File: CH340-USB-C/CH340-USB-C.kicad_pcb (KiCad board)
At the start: 2 copper layers, 37.2 x 19.5 mm, 25 parts, among them J1 USB_C_Receptacle_USB2.0, J2 Conn_01x05_Female, SW1 SW_Push_SPDT, U1 XC6206PxxxMR, U2 CH340N

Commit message: fix 電路板零件屬性及用料
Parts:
- U1: value XC6206PxxxMR -> XC6206P332MR
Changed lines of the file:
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@@
     (property "Sheetfile" "CH340-USB-C.kicad_sch")
     (property "Sheetname" "")
-    (attr exclude_from_pos_files)
+    (property "exclude_from_bom" "")
+    (attr exclude_from_pos_files exclude_from_bom)
     (fp_text reference "TP2" (at 0 -1.998) (layer "F.SilkS") hide
       (effects (font (size 1 1) (thickness 0.15)))
@@
     (property "Sheetfile" "CH340-USB-C.kicad_sch")
     (property "Sheetname" "")
-    (attr exclude_from_pos_files)
+    (property "exclude_from_bom" "")
+    (attr exclude_from_pos_files exclude_from_bom)
     (fp_text reference "TP6" (at 0 -1.998) (layer "F.SilkS") hide
       (effects (font (size 1 1) (thickness 0.15)))
@@
     (fp_line (start 1 -0.625) (end 1 0.625) (layer "F.Fab") (width 0.1))
     (fp_line (start -1 -0.625) (end 1 -0.625) (layer "F.Fab") (width 0.1))
-    (pad "1" smd roundrect (at -0.9125 0) (size 1.025 1.4) (layers "F.Cu" "F.Paste" "F.Mask") (roundrect_rratio 0.243902)
+    (pad "1" smd roundrect (at -0.9125 0) (size 1.025 1.4) (layers "F.Cu" "F.Paste" "F.Mask") (roundrect_rratio 0.243902439)
       (net 10 "Net-(D3-Pad2)") (pintype "passive"))
-    (pad "2" smd roundrect (at 0.9125 0) (size 1.025 1.4) (layers "F.Cu" "F.Paste" "F.Mask") (roundrect_rratio 0.243902)
+    (pad "2" smd roundrect (at 0.9125 0) (size 1.025 1.4) (layers "F.Cu" "F.Paste" "F.Mask") (roundrect_rratio 0.243902439)
       (net 4 "VCC") (pintype "passive"))
     (model "${KICAD6_3DMODEL_DIR}/Resistor_SMD.3dshapes/R_0805_2012Metric.wrl"
@@
     (fp_line (start 1 -0.625) (end 1 0.625) (layer "F.Fab") (width 0.1))
     (fp_line (start -1 0.625) (end -1 -0.625) (layer "F.Fab") (width 0.1))
-    (pad "1" smd roundrect (at -0.9125 0 180) (size 1.025 1.4) (layers "F.Cu" "F.Paste" "F.Mask") (roundrect_rratio 0.243902)
+    (pad "1" smd roundrect (at -0.9125 0 180) (size 1.025 1.4) (layers "F.Cu" "F.Paste" "F.Mask") (roundrect_rratio 0.243902439)
       (net 2 "GND") (pintype "passive"))
-    (pad "2" smd roundrect (at 0.9125 0 180) (size 1.025 1.4) (layers "F.Cu" "F.Paste" "F.Mask") (roundrect_rratio 0.243902)
+    (pad "2" smd roundrect (at 0.9125 0 180) (size 1.025 1.4) (layers "F.Cu" "F.Paste" "F.Mask") (roundrect_rratio 0.243902439)
       (net 16 "/CC2") (pintype "passive"))
     (model "${KICAD6_3DMODEL_DIR}/Resistor_SMD.3dshapes/R_0805_2012Metric.wrl"
@@
     (property "Sheetfile" "CH340-USB-C.kicad_sch")
     (property "Sheetname" "")
-    (attr exclude_from_pos_files)
+    (property "exclude_from_bom" "")
+    (attr exclude_from_pos_files exclude_from_bom)
     (fp_text reference "TP5" (at 0 -1.998) (layer "F.SilkS") hide
       (effects (font (size 1 1) (thickness 0.15)))
@@
     (fp_line (start -1 -0.625) (end 1 -0.625) (layer "F.Fab") (width 0.1))
     (fp_line (start 1 -0.625) (end 1 0.625) (layer "F.Fab") (width 0.1))
-    (pad "1" smd roundrect (at -0.9125 0 180) (size 1.025 1.4) (layers "F.Cu" "F.Paste" "F.Mask") (roundrect_rratio 0.243902)
+    (pad "1" smd roundrect (at -0.9125 0 180) (size 1.025 1.4) (layers "F.Cu" "F.Paste" "F.Mask") (roundrect_rratio 0.243902439)
       (net 2 "GND") (pintype "passive"))
-    (pad "2" smd roundrect (at 0.9125 0 180) (size 1.025 1.4) (layers "F.Cu" "F.Paste" "F.Mask") (roundrect_rratio 0.243902)
+    (pad "2" smd roundrect (at 0.9125 0 180) (size 1.025 1.4) (layers "F.Cu" "F.Paste" "F.Mask") (roundrect_rratio 0.243902439)
       (net 12 "/CC1") (pintype "passive"))
     (model "${KICAD6_3DMODEL_DIR}/Resistor_SMD.3dshapes/R_0805_2012Metric.wrl"
@@
     (descr "SOT, 3 Pin (https://www.jedec.org/system/files/docs/to-236h.pdf variant AB), generated with kicad-footprint-generator ipc_gullwing_generator.py")
     (tags "SOT TO_SOT_SMD")
-    (property "LCSC" "C161345")
+    (property "LCSC" "C5446")
     (property "Sheetfile" "CH340-USB-C.kicad_sch")
     (property "Sheetname" "")
@@
       (effects (font (size 1 1) (thickness 0.15)))
     )
-    (fp_text value "XC6206PxxxMR" (at -4.8225 -0.623332 180) (layer "F.Fab")
+    (fp_text value "XC6206P332MR" (at -4.8225 -0.623332 180) (layer "F.Fab")
       (effects (font (size 1 1) (thickness 0.15)))
     )
@@
     (property "Sheetfile" "CH340-USB-C.kicad_sch")
     (property "Sheetname" "")
-    (attr exclude_from_pos_files)
+    (property "exclude_from_bom" "")
+    (attr exclude_from_pos_files exclude_from_bom)
     (fp_text reference "TP1" (at 0 -1.998) (layer "F.SilkS") hide
       (effects (font (size 1 1) (thickness 0.15)))
@@
     (fp_line (start 1 0.625) (end -1 0.625) (layer "F.Fab") (width 0.1))
     (fp_line (start -1 0.625) (end -1 -0.625) (layer "F.Fab") (width 0.1))
-    (pad "1" smd roundrect (at -0.9125 0) (size 1.025 1.4) (layers "F.Cu" "F.Paste" "F.Mask") (roundrect_rratio 0.243902)
+    (pad "1" smd roundrect (at -0.9125 0) (size 1.025 1.4) (layers "F.Cu" "F.Paste" "F.Mask") (roundrect_rratio 0.243902439)
       (net 6 "Net-(D1-Pad2)") (pintype "passive"))
-    (pad "2" smd roundrect (at 0.9125 0) (size 1.025 1.4) (layers "F.Cu" "F.Paste" "F.Mask") (roundrect_rratio 0.243902)
+    (pad "2" smd roundrect (at 0.9125 0) (size 1.025 1.4) (layers "F.Cu" "F.Paste" "F.Mask") (roundrect_rratio 0.243902439)
       (net 4 "VCC") (pintype "passive"))
     (model "${KICAD6_3DMODEL_DIR}/Resistor_SMD.3dshapes/R_0805_2012Metric.wrl"
@@
     (property "Sheetfile" "CH340-USB-C.kicad_sch")
     (property "Sheetname" "")
-    (attr exclude_from_pos_files)
+    (property "exclude_from_bom" "")
+    (attr exclude_from_pos_files exclude_from_bom)
     (fp_text reference "TP4" (at 0 -1.998) (layer "F.SilkS") hide
       (effects (font (size 1 1) (thickness 0.15)))
@@
     (property "Sheetfile" "CH340-USB-C.kicad_sch")
     (property "Sheetname" "")
-    (attr exclude_from_pos_files)
+    (property "exclude_from_bom" "")
+    (attr exclude_from_pos_files exclude_from_bom)
     (fp_text reference "TP3" (at 0 -1.998) (layer "F.SilkS") hide
       (effects (font (size 1 1) (thickness 0.15)))
@@
     (fp_line (start -1 0.625) (end -1 -0.625) (layer "F.Fab") (width 0.1))
     (fp_line (start 1 0.625) (end -1 0.625) (layer "F.Fab") (width 0.1))
-    (pad "1" smd roundrect (at -0.9125 0) (size 1.025 1.4) (layers "F.Cu" "F.Paste" "F.Mask") (roundrect_rratio 0.243902)
+    (pad "1" smd roundrect (at -0.9125 0) (size 1.025 1.4) (layers "F.Cu" "F.Paste" "F.Mask") (roundrect_rratio 0.243902439)
       (net 8 "Net-(D2-Pad2)") (pintype "passive"))
-    (pad "2" smd roundrect (at 0.9125 0) (size 1.025 1.4) (layers "F.Cu" "F.Paste" "F.Mask") (roundrect_rratio 0.243902)
+    (pad "2" smd roundrect (at 0.9125 0) (size 1.025 1.4) (layers "F.Cu" "F.Paste" "F.Mask") (roundrect_rratio 0.243902439)
       (net 4 "VCC") (pintype "passive"))
     (model "${KICAD6_3DMODEL_DIR}/Resistor_SMD.3dshapes/R_0805_2012Metric.wrl"
@@
     (descr "KiCad Logo")
     (tags "Logo KiCad")
-    (attr exclude_from_pos_files exclude_from_bom)
+    (attr board_only exclude_from_pos_files exclude_from_bom)
     (fp_text reference "REF**" (at 0 5.08) (layer "B.SilkS") hide
       (effects (font (size 1 1) (thickness 0.15)) (justify mirror))
@@
     (property "Sheetfile" "CH340-USB-C.kicad_sch")
     (property "Sheetname" "")
-    (attr smd)
+    (property "exclude_from_bom" "")
+    (attr smd exclude_from_pos_files exclude_from_bom)
     (fp_text reference "J2" (at -11.384 -12.34 unlocked) (layer "B.SilkS")
       (effects (font (size 1 1) (thickness 0.15)) (justify mirror))

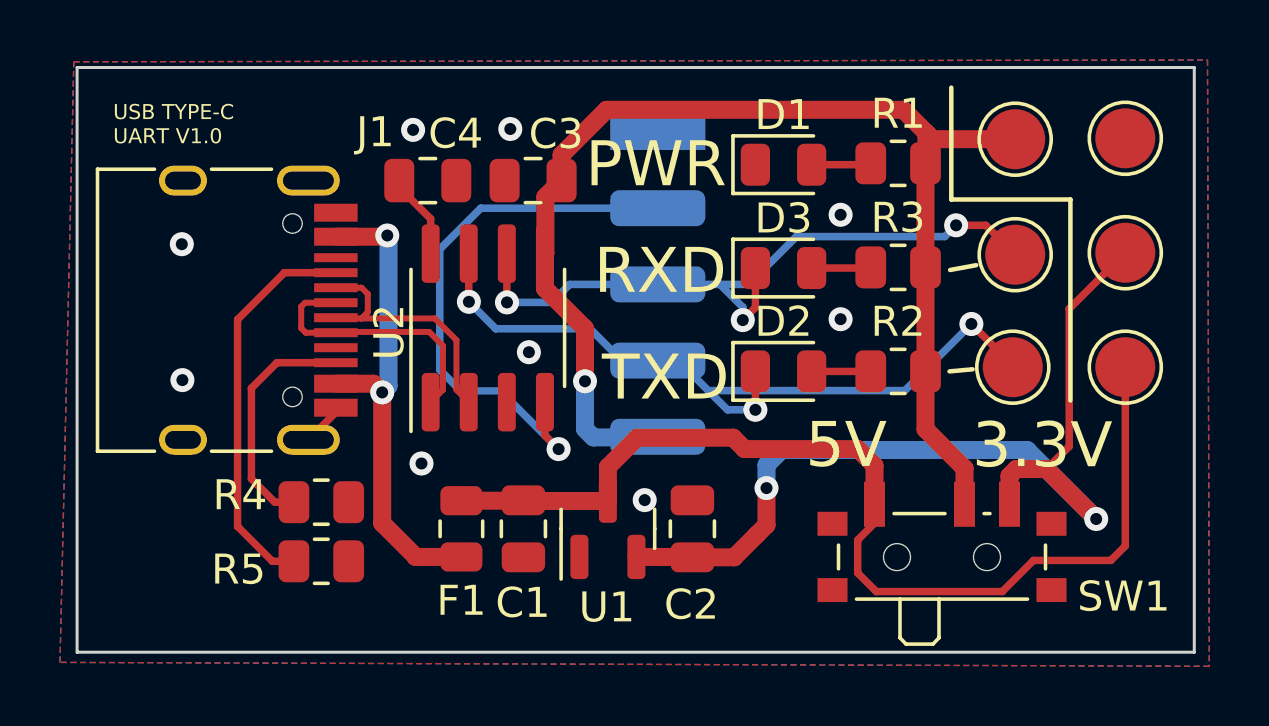
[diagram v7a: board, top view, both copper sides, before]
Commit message: 新增功能
1.可以對外輸出電源
2.可以切換電壓准位
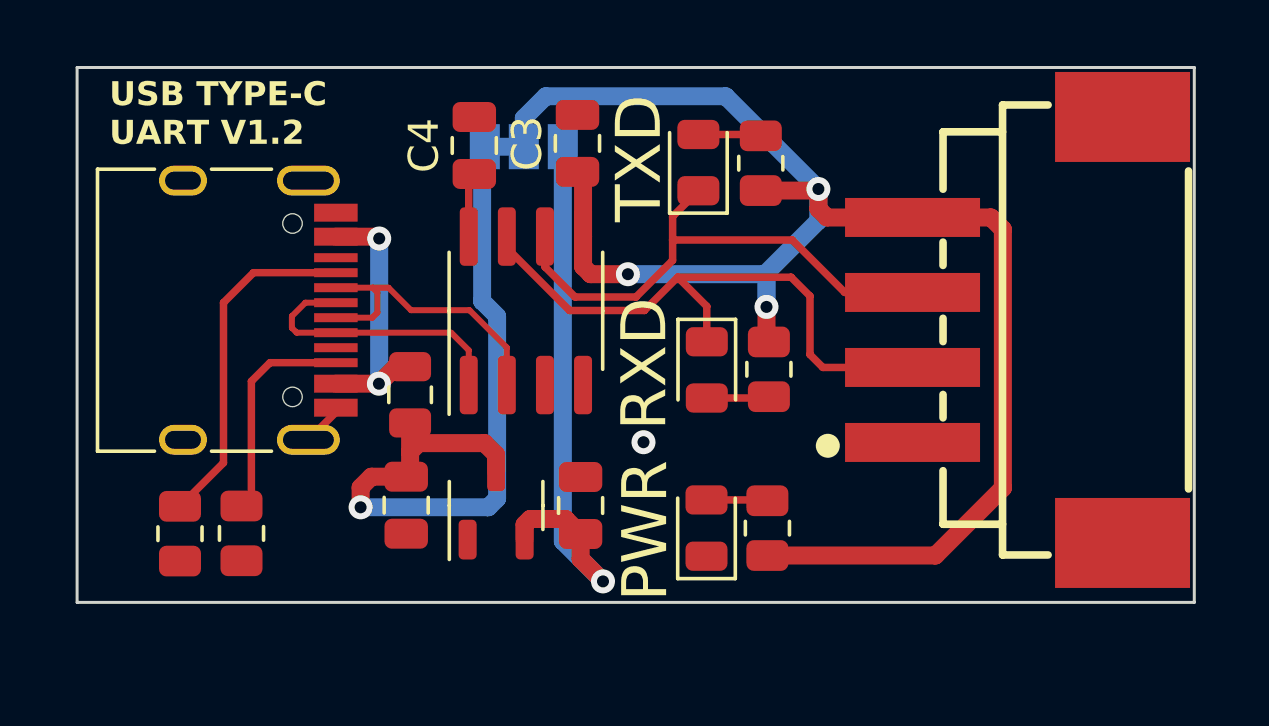
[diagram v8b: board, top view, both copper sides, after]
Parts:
- removed TP1, TP2, TP3, TP4, TP5, TP6: TestPoint, TestPoint:TestPoint_Pad_D2.0mm
- J2: value Conn_01x05_Female -> Conn_01x04_MountingPin; footprint Connector_PinSocket_2.54mm:PinSocket_1x05P_2.54mm_Horizontal_SMD -> MY-Connector_JST:JST_PH_S4B-XH-SM4-TB_1x04-1MP_P2.50mm_Horizontal; moved to F.Cu
- R1: value 330 -> 1k
- SW1: footprint Button_Switch_SMD:SW_SPDT_PCM12 -> Jumper:SolderJumper-3_P1.3mm_Bridged12_Pad1.0x1.5mm; moved to B.Cu
- U1: value XC6206P332MR -> XC6206PxxxMR; footprint Package_TO_SOT_SMD:SOT-23 -> Package_TO_SOT_SMD:SOT-23-3
- moved REF** 25.6 mm to (96.6, 97.0), turned to -90 degrees
- moved J2 23.5 mm to (100.1, 105.9), turned to 90 degrees
- moved SW1 19.3 mm to (77.8, 91.1)
- moved R1 12.9 mm to (85.9, 103.8), turned to -90 degrees
- moved D1 12.4 mm to (83.9, 103.8), turned to 90 degrees
- moved R3 5.75 mm to (85.7, 91.6), turned to -90 degrees
- moved R5 4.80 mm to (66.4, 104.0), turned to 90 degrees
- moved F1 4.78 mm to (74.0, 99.4), turned to -90 degrees
- moved D3 4.52 mm to (83.6, 91.6), turned to 90 degrees
- moved R2 4.31 mm to (86.0, 98.5), turned to 90 degrees
- moved C1 3.99 mm to (73.9, 103.0)
- moved U1 3.81 mm to (76.9, 103.0)
- moved C2 3.81 mm to (79.7, 103.0)
- moved R4 2.86 mm to (68.4, 104.0), turned to 90 degrees
- moved D2 2.56 mm to (83.9, 98.5), turned to -90 degrees
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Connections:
- J2 pad 2: /~{RTS} -> /RXD
- J2 pad 4: /RXD -> VCC
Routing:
- net /~{RTS}: track 18.7 -> 0.00 mm, vias 1 -> 0
- net VCC: track 41.5 -> 54.1 mm, vias 1 -> 3
- net +3V3: track 31.9 -> 19.6 mm, vias 2 -> 1
- net +5V: track 35.3 -> 24.5 mm, vias 0 -> 1
- net Net-(F1-Pad1): track 16.2 -> 9.02 mm
- net /TXD: track 23.5 -> 17.6 mm, vias 3 -> 0
- net /RXD: track 25.6 -> 20.2 mm, vias 3 -> 0
- net /CC1: track 13.2 -> 11.5 mm
- net /USBD-: track 8.62 -> 10.1 mm
- net /3V3: track 2.87 -> 2.16 mm
- net /CC2: track 7.97 -> 7.37 mm
- net GND: vias 9 -> 1
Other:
- board size 37.2 x 19.5 mm -> 37.2 x 17.8 mm
- board text added: "3V3"
- board text added: "USB TYPE-C UART V1.2"
- board text removed: "3.3V"
- board text removed: "GND"
- board text removed: "USB TYPE-C UART V1.0"
- board text removed: "VCC"
- board text removed: "~{RTS}"
